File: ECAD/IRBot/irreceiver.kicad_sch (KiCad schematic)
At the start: 35 parts, among them U1 LM358

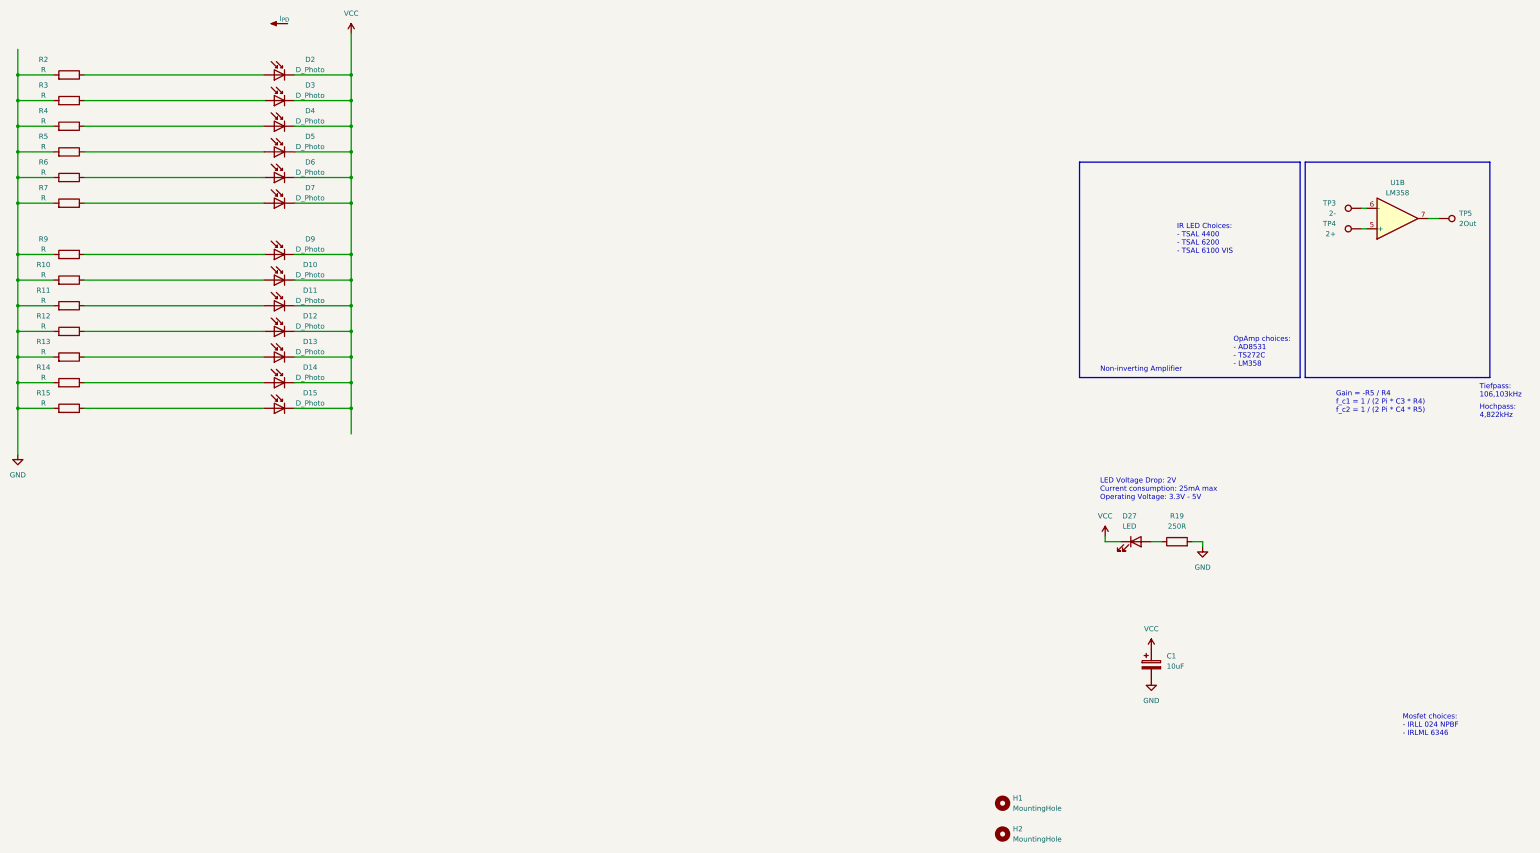
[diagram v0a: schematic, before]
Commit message: Fix broken schematic
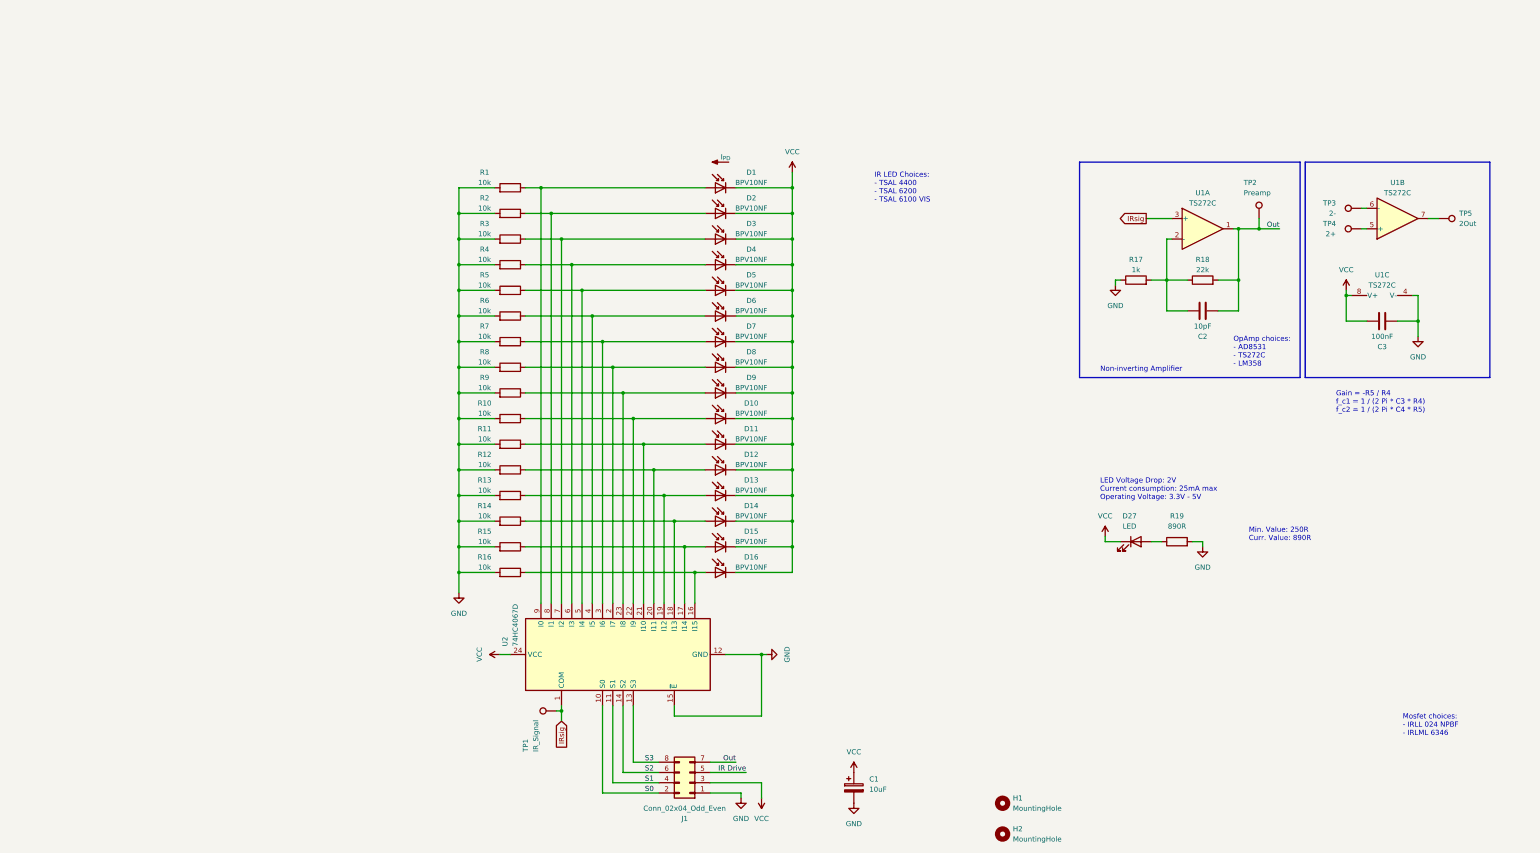
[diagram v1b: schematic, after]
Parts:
- added C2: 10pF, Capacitor_SMD:C_0805_2012Metric_Pad1.18x1.45mm_HandSolder, symbol Device:C
- added C3: 100nF, Capacitor_SMD:C_0805_2012Metric_Pad1.18x1.45mm_HandSolder, symbol Device:C
- added D1, D16, D8: BPV10NF, LED_THT:LED_D5.0mm_Horizontal_O3.81mm_Z3.0mm, symbol Device:D_Photo
- added J1: Conn_02x04_Odd_Even, Connector_PinHeader_2.54mm:PinHeader_2x04_P2.54mm_Vertical, symbol Connector_Generic:Conn_02x04_Odd_Even
- added R1, R16, R8: 10k, Resistor_SMD:R_0805_2012Metric_Pad1.20x1.40mm_HandSolder, symbol Device:R
- added R17: 1k, Resistor_SMD:R_0805_2012Metric_Pad1.20x1.40mm_HandSolder, symbol Device:R
- added R18: 22k, Resistor_SMD:R_0805_2012Metric_Pad1.20x1.40mm_HandSolder, symbol Device:R
- added TP1: IR_Signal, TestPoint:TestPoint_Pad_D1.0mm, symbol Connector:TestPoint
- added TP2: Preamp, TestPoint:TestPoint_Pad_D1.0mm, symbol Connector:TestPoint
- added unit 3 of U1
- added unit 1 of U1
- added U2: 74HC4067D, Package_SO:SOIC-24W_7.5x15.4mm_P1.27mm, symbol 74xx:CD74HC4067M
- D10, D11, D12, D13, D14, D15, D2, D3, D4, D5, D6, D7, D9: value D_Photo -> BPV10NF
- R10, R11, R12, R13, R14, R15, R2, R3, R4, R5, R6, R7, R9: value R -> 10k
- R19: value 250R -> 890R
- U1: value LM358 -> TS272C
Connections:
- net GND: now also C3.2, J1.1 (Pin_1), R1.2, R16.2, R17.1, R8.2, U1.4 (V-), U2.12 (GND), U2.15 (~{E})
- net VCC: now also C3.1, D1.1 (K), D16.1 (K), D8.1 (K), J1.3 (Pin_3), U1.8 (V+), U2.24 (VCC)
- net at D4.2 (A), R4.1: now also U2.6 (I3)
- net at D10.2 (A), R10.1: now also U2.22 (I9)
- net at D11.2 (A), R11.1: now also U2.21 (I10)
- net at D7.2 (A), R7.1: now also U2.3 (I6)
- net at D5.2 (A), R5.1: now also U2.5 (I4)
- net at D2.2 (A), R2.1: now also U2.8 (I1)
- net at D13.2 (A), R13.1: now also U2.19 (I12)
- net at D3.2 (A), R3.1: now also U2.7 (I2)
- net at D15.2 (A), R15.1: now also U2.17 (I14)
- net at D9.2 (A), R9.1: now also U2.23 (I8)
- net at D12.2 (A), R12.1: now also U2.20 (I11)
- net at D6.2 (A), R6.1: now also U2.4 (I5)
- net at D14.2 (A), R14.1: now also U2.18 (I13)
- new net: D1.2 (A), R1.1, U2.9 (I0)
- new net: D16.2 (A), R16.1, U2.16 (I15)
- new net: D8.2 (A), R8.1, U2.2 (I7)
- new net: C2.1, R17.2, R18.1, U1.2 (-)
- new net IR Drive: J1.5 (Pin_5)
- new net IRsig: TP1.1, U1.3 (+), U2.1 (COM)
- new net Out: C2.2, J1.7 (Pin_7), R18.2, TP2.1, U1.1
- new net S0: J1.2 (Pin_2), U2.10 (S0)
- new net S1: J1.4 (Pin_4), U2.11 (S1)
- new net S2: J1.6 (Pin_6), U2.14 (S2)
- new net S3: J1.8 (Pin_8), U2.13 (S3)
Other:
- note added: "Min. Value: 250R Curr. Value: 890R"
- note removed: "Hochpass: 4,822kHz"
- note removed: "Tiefpass: 106,103kHz"
- moved on the sheet: C1, D10, D11, D12, D13, D14, D15, D2, D3, D4, D5, D6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

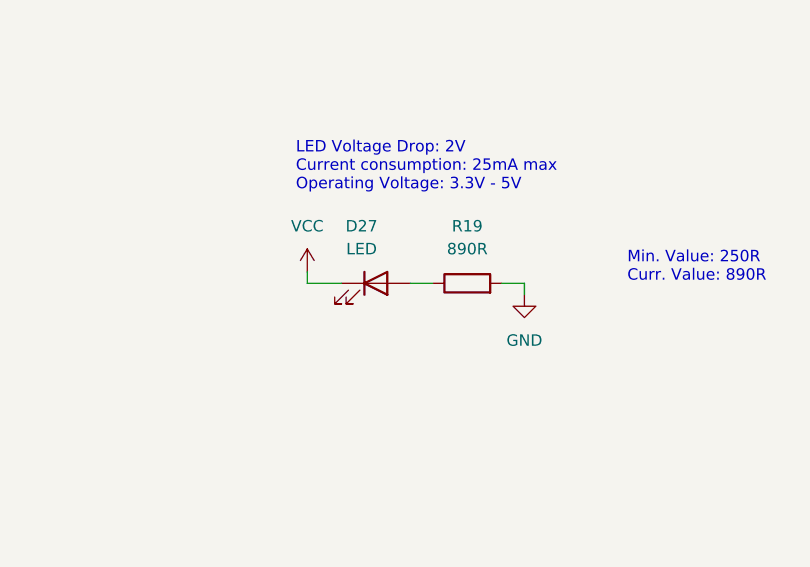
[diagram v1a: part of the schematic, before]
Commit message: Update Matlab Code for new Graphics
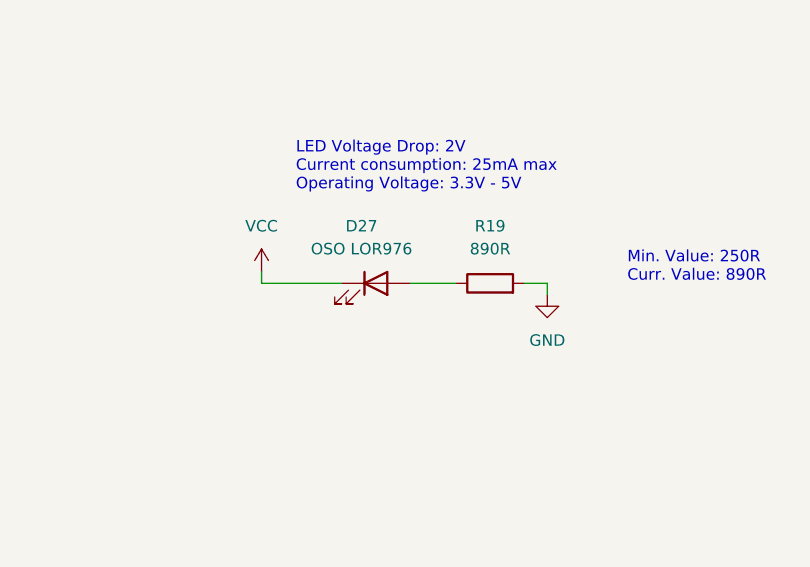
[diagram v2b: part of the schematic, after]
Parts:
- D27: value LED -> OSO LOR976
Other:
- moved on the sheet: R19
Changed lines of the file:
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@@
     (stroke (width 0) (type default))
   )
-  (wire (pts (xy 182.88 111.76) (xy 179.07 111.76))
+  (wire (pts (xy 182.88 111.76) (xy 173.99 111.76))
     (stroke (width 0) (type default))
   )
@@
     (stroke (width 0) (type default))
   )
-  (wire (pts (xy 203.2 113.03) (xy 203.2 111.76))
+  (wire (pts (xy 205.74 113.03) (xy 205.74 111.76))
     (stroke (width 0) (type default))
   )
@@
     (stroke (width 0) (type default))
   )
-  (wire (pts (xy 203.2 111.76) (xy 200.66 111.76))
+  (wire (pts (xy 205.74 111.76) (xy 203.2 111.76))
     (stroke (width 0) (type default))
   )
@@
     (stroke (width 0) (type default))
   )
-  (wire (pts (xy 190.5 111.76) (xy 193.04 111.76))
+  (wire (pts (xy 190.5 111.76) (xy 195.58 111.76))
     (stroke (width 0) (type default))
   )
@@
     (stroke (width 0) (type default))
   )
-  (wire (pts (xy 179.07 111.76) (xy 179.07 110.49))
+  (wire (pts (xy 173.99 111.76) (xy 173.99 110.49))
     (stroke (width 0) (type default))
   )
@@
       (effects (font (size 1.27 1.27)))
     )
-    (property "Value" "LED" (at 185.1025 107.95 0)
+    (property "Value" "OSO LOR976" (at 185.1025 107.95 0)
       (effects (font (size 1.27 1.27)))
     )
@@
     )
   )
-  (symbol (lib_id "power:VCC") (at 179.07 110.49 0) (unit 1)
-    (in_bom yes) (on_board yes) (dnp no) (fields_autoplaced)
-    (property "Reference" "#PWR05" (at 179.07 114.3 0)
-      (effects (font (size 1.27 1.27)) hide)
-    )
-    (property "Value" "VCC" (at 179.07 105.41 0)
-      (effects (font (size 1.27 1.27)))
-    )
-    (property "Footprint" "" (at 179.07 110.49 0)
-      (effects (font (size 1.27 1.27)) hide)
-    )
-    (property "Datasheet" "" (at 179.07 110.49 0)
+  (symbol (lib_id "power:VCC") (at 173.99 110.49 0) (unit 1)
+    (in_bom yes) (on_board yes) (dnp no) (fields_autoplaced)
+    (property "Reference" "#PWR05" (at 173.99 114.3 0)
+      (effects (font (size 1.27 1.27)) hide)
+    )
+    (property "Value" "VCC" (at 173.99 105.41 0)
+      (effects (font (size 1.27 1.27)))
+    )
+    (property "Footprint" "" (at 173.99 110.49 0)
+      (effects (font (size 1.27 1.27)) hide)
+    )
+    (property "Datasheet" "" (at 173.99 110.49 0)
       (effects (font (size 1.27 1.27)) hide)
     )
@@
     )
   )
-  (symbol (lib_id "Device:R") (at 196.85 111.76 90) (unit 1)
-    (in_bom yes) (on_board yes) (dnp no) (fields_autoplaced)
-    (property "Reference" "R19" (at 196.85 105.41 90)
-      (effects (font (size 1.27 1.27)))
-    )
-    (property "Value" "890R" (at 196.85 107.95 90)
-      (effects (font (size 1.27 1.27)))
-    )
-    (property "Footprint" "Resistor_SMD:R_0805_2012Metric_Pad1.20x1.40mm_HandSolder" (at 196.85 113.538 90)
-      (effects (font (size 1.27 1.27)) hide)
-    )
-    (property "Datasheet" "~" (at 196.85 111.76 0)
+  (symbol (lib_id "Device:R") (at 199.39 111.76 90) (unit 1)
+    (in_bom yes) (on_board yes) (dnp no) (fields_autoplaced)
+    (property "Reference" "R19" (at 199.39 105.41 90)
+      (effects (font (size 1.27 1.27)))
+    )
+    (property "Value" "890R" (at 199.39 107.95 90)
+      (effects (font (size 1.27 1.27)))
+    )
+    (property "Footprint" "Resistor_SMD:R_0805_2012Metric_Pad1.20x1.40mm_HandSolder" (at 199.39 113.538 90)
+      (effects (font (size 1.27 1.27)) hide)
+    )
+    (property "Datasheet" "~" (at 199.39 111.76 0)
       (effects (font (size 1.27 1.27)) hide)
     )
@@
     )
   )
-  (symbol (lib_id "power:GND") (at 203.2 113.03 0) (mirror y) (unit 1)
-    (in_bom yes) (on_board yes) (dnp no) (fields_autoplaced)
-    (property "Reference" "#PWR06" (at 203.2 119.38 0)
-      (effects (font (size 1.27 1.27)) hide)
-    )
-    (property "Value" "GND" (at 203.2 118.11 0)
-      (effects (font (size 1.27 1.27)))
-    )
-    (property "Footprint" "" (at 203.2 113.03 0)
-      (effects (font (size 1.27 1.27)) hide)
-    )
-    (property "Datasheet" "" (at 203.2 113.03 0)
-      (effects (font (size 1.27 1.27)) hide)
-    )
+  (symbol (lib_id "power:GND") (at 205.74 113.03 0) (mirror y) (unit 1)
+    (in_bom yes) (on_board yes) (dnp no) (fields_autoplaced)
+    (property "Reference" "#PWR06" (at 205.74 119.38 0)
+      (effects (font (size 1.27 1.27)) hide)
+    )
+    (property "Value" "GND" (at 205.74 118.11 0)
+      (effects (font (size 1.27 1.27)))
+    )
+    (property "Footprint" "" (at 205.74 113.03 0)
+      (effects (font (size 1.27 1.27)) hide)
+    )
+    (property "Datasheet" "" (at 205.74 113.03 0)
+      (effects (font (size 1.27 1.27)) hide)
+    )
